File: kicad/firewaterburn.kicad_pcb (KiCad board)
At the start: 2 copper layers, 159.6 x 104.7 mm, 85 parts, among them J1 AudioJack2_SwitchT, J2 AudioJack2_SwitchT, J3 AudioJack2_SwitchT, J4 AudioJack2_SwitchT, J5 AudioJack2_SwitchT, J6 AudioJack2_SwitchT, J7 R61529 LCD, J9 Conn_01x03, P1 USB_C_Plug_USB2.0, Q1 DMN61D9UWQ-13, Q2 DMP31D0U-7, Q3 SS8050-G, Q4 SS8050-G, Q6 DMN2004WK-7, SW1 SW_MEC_5G, SW2 SW_MEC_5G, U1 RT9471GQW, U2 MCP1663T-E/MNY, U3 MCP1603-330I/MC, U4 ESP32-S3-Rx, U5 CP2102N-Axx-xQFN28

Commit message: route complete pcb
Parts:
- removed J9: Conn_01x03, z_connector:Molex_KK-254_AE-6410-03A_1x03_P2.54mm_Vertical
- removed JP2: SolderJumper_3_Open, Jumper:SolderJumper-3_P1.3mm_Open_Pad1.0x1.5mm_NumberLabels
- removed Q6: DMN2004WK-7, Package_TO_SOT_SMD:SOT-323_SC-70
- removed R42, R43: 0R, Resistor_SMD:R_0603_1608Metric
- added J8: R61529 LCD, z_connector:FPC_BOTTOM_20POS_Würth_68712014522, F.Cu at (176.2, 115.0)
- added Q5: DMN2004WK-7, Package_TO_SOT_SMD:SOT-323_SC-70, F.Cu at (103.9, 91.8)
- added R30: 0R, Resistor_SMD:R_0603_1608Metric, F.Cu at (122.7, 130.0)
- added R31: 0R, Resistor_SMD:R_0603_1608Metric, F.Cu at (117.0, 130.0)
- added R32: 10k, Resistor_SMD:R_0603_1608Metric, F.Cu at (163.6, 122.8)
- J3: value AudioJack2_SwitchT -> Conn_01x03; footprint z_connector:MJ-2523 -> z_connector:Molex_KK-254_AE-6410-03A_1x03_P2.54mm_Vertical
- J7: value R61529 LCD -> AudioJack2_SwitchT; footprint z_connector:62684-402100ALF -> z_connector:MJ-2523
- R10, R12: value 3k4 -> 4k42
- R11: value 4k42 -> 3k4
- R13, R17: value 10k -> 3k4
- R18: value 5k23 -> 10k
- R19: value 30k1 -> 0R
- R20: value 2k2 -> 5k23
- R21: value 2k2 -> 30k1
- R22: value 1050k -> 2k2
- R23: value 120k -> 2k2
- R24, R25: value 10k -> 0R
- R26: value 0R -> 1050k
- R27: value 0R -> 120k
- R29, R41: value 0R -> 10k
- R33: value 22k1 -> 0R
- R34: value 47k5 -> 0R
- R35: value 2k -> 22k1
- R36: value 1M -> 47k5
- R37: value 10k -> 2k
- R38: value 3k4 -> 0R
- R40: value 0R -> 1M
- R9: value 4k42 -> 10k
- U1: footprint Package_DFN_QFN:WQFN-24-1EP_4x4mm_P0.5mm_EP2.6x2.6mm_ThermalVias -> z_ic:WQFN-24-1EP_4x4mm_P0.5mm_EP2.6x2.6mm_ThermalVias
- moved R35 92.8 mm to (105.4, 82.8)
- moved R37 88.7 mm to (105.4, 86.0)
- moved C14 88.3 mm to (107.0, 80.2), turned to 90 degrees
- moved R16 87.1 mm to (181.4, 68.3), turned to 90 degrees
- moved D1 86.6 mm to (111.8, 75.0)
- moved R19 85.8 mm to (112.6, 112.2), turned to 90 degrees
- moved R41 85.4 mm to (102.3, 89.2), turned to 180 degrees
- moved R36 84.4 mm to (105.4, 84.4), turned to 180 degrees
- moved U5 83.2 mm to (111.2, 85.9), turned to -90 degrees
- moved C3 80.4 mm to (110.0, 105.5), turned to 90 degrees
- moved P1 80.4 mm to (111.8, 65.2)
- moved C13 80.1 mm to (108.6, 80.2), turned to 90 degrees
- moved R2 76.6 mm to (132.1, 121.2), turned to -90 degrees
- moved C2 75.8 mm to (109.2, 109.8), turned to 180 degrees
- moved R15 74.8 mm to (169.4, 65.2), turned to 90 degrees
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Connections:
- J4 pad T: /OUTPUT/probe5 -> /OUTPUT/probe2
- J5 pad T: /OUTPUT/probe3 -> /OUTPUT/probe5
- J6 pad T: /OUTPUT/probe6 -> /OUTPUT/probe3
- Q2 pad 3: Net-(J9-Pad2) -> Net-(J3-Pad2)
- R10 pad 1: /OUTPUT/probe2 -> +3V3
- R10 pad 2: GND -> /OUTPUT/probe2
- R11 pad 1: +3V3 -> /OUTPUT/probe2
- R11 pad 2: /OUTPUT/probe5 -> GND
- R12 pad 1: /OUTPUT/probe5 -> +3V3
- R12 pad 2: GND -> /OUTPUT/probe5
- R13 pad 1: +3V3 -> /OUTPUT/probe5
- R13 pad 2: /OUTPUT/TACHO -> GND
- R17 pad 1: /mcu_n_tft/CHR_INT -> /OUTPUT/probe6
- R17 pad 2: +3V3 -> GND
- R18 pad 1: Net-(C5-Pad1) -> /mcu_n_tft/CHR_INT
- R18 pad 2: Net-(R18-Pad2) -> +3V3
- R19 pad 1: Net-(R18-Pad2) -> VBUS
- R19 pad 2: GND -> Net-(C1-Pad1)
- R20 pad 1: Net-(D2-Pad1) -> Net-(C5-Pad1)
- R20 pad 2: /power unit/STAT -> Net-(R20-Pad2)
- R21 pad 1: Net-(D3-Pad1) -> Net-(R20-Pad2)
- R21 pad 2: /power unit/~{PG} -> GND
- R22 pad 1: +12V -> Net-(D2-Pad1)
- R22 pad 2: Net-(R22-Pad2) -> /power unit/STAT
- R23 pad 1: Net-(R22-Pad2) -> Net-(D3-Pad1)
- R23 pad 2: GND -> /power unit/~{PG}
- R24 pad 1: Net-(Q3-Pad1) -> VAA
- R24 pad 2: /USB<->UART/DTS -> Net-(C6-Pad1)
- R25 pad 1: Net-(Q4-Pad1) -> VS
- R25 pad 2: /mcu_n_tft/RTS -> Net-(C7-Pad1)
- R26 pad 1: /mcu_n_tft/EN -> +12V
- R26 pad 2: Net-(Q3-Pad3) -> Net-(R26-Pad2)
- R27 pad 1: /mcu_n_tft/BOOT -> Net-(R26-Pad2)
- R27 pad 2: Net-(Q4-Pad3) -> GND
- R28 pad 1: +3V3 -> Net-(Q3-Pad1)
- R28 pad 2: /mcu_n_tft/EN -> /USB<->UART/DTS
- R29 pad 1: Net-(R29-Pad1) -> Net-(Q4-Pad1)
- R29 pad 2: +3V3 -> /mcu_n_tft/RTS
- R33 pad 1: VBUS -> Net-(R33-Pad1)
- R33 pad 2: Net-(R33-Pad2) -> +3V3
- R34 pad 1: Net-(R33-Pad2) -> +3V3
- R34 pad 2: GND -> Net-(J8-Pad1)
- R35 pad 1: +3V3 -> VBUS
- R36 pad 1: GND -> Net-(R35-Pad2)
- R36 pad 2: Net-(Q6-Pad1) -> GND
- R37 pad 1: /USB<->UART/CHREN -> +3V3
- R37 pad 2: VBUS -> Net-(R37-Pad2)
- R38 pad 1: /OUTPUT/probe6 -> +3V3
- R38 pad 2: GND -> Net-(R38-Pad2)
- R39 pad 1: VBUS -> Net-(Q5-Pad1)
- R39 pad 2: Net-(C1-Pad1) -> /USB<->UART/CHREN_
- R40 pad 1: VAA -> GND
- R40 pad 2: Net-(C6-Pad1) -> Net-(Q5-Pad1)
- R41 pad 1: VS -> /USB<->UART/CHREN
- R41 pad 2: Net-(C7-Pad1) -> VBUS
- R9 pad 2: /OUTPUT/probe2 -> /OUTPUT/TACHO
- TH1 pad 1: Net-(R18-Pad2) -> Net-(R20-Pad2)
- U1 pad 11: Net-(R18-Pad2) -> Net-(R20-Pad2)
- U2 pad 1: Net-(R22-Pad2) -> Net-(R26-Pad2)
- U4 pad 12: /OUTPUT/probe5 -> /OUTPUT/probe4
- U4 pad 17: /OUTPUT/probe6 -> /OUTPUT/probe1
- U4 pad 18: /OUTPUT/TACHO -> /OUTPUT/PWM
- U4 pad 19: /OUTPUT/PWM -> /OUTPUT/TACHO
- U4 pad 2: Net-(R29-Pad1) -> Net-(R33-Pad1)
- U4 pad 23: /mcu_n_tft/~{PD} -> /USB<->UART/CHR1
- U4 pad 4: /OUTPUT/probe1 -> /OUTPUT/probe6
- U4 pad 5: /OUTPUT/probe2 -> /OUTPUT/probe3
- U4 pad 6: /OUTPUT/probe3 -> /OUTPUT/probe5
- U4 pad 7: /OUTPUT/probe4 -> /OUTPUT/probe2
- U4 pad 8: /USB<->UART/CHR1 -> /mcu_n_tft/~{PD}
- U5 pad 6: Net-(JP2-Pad2) -> Net-(R38-Pad2)
- U5 pad 8: Net-(R33-Pad2) -> Net-(R35-Pad2)
- U5 pad 9: Net-(R35-Pad2) -> Net-(R37-Pad2)
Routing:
- net GND: track 0.00 -> 527.7 mm, vias 0 -> 40
- net +3V3: track 0.00 -> 245.0 mm, vias 0 -> 17
- net /OUTPUT/probe1: track 0.00 -> 95.1 mm
- net /OUTPUT/probe4: track 0.00 -> 80.7 mm, vias 0 -> 2
- net VBUS: track 0.00 -> 79.0 mm, vias 0 -> 2
- net /mcu_n_tft/RTS: track 0.00 -> 78.1 mm, vias 0 -> 2
- net /OUTPUT/probe2: track 0.00 -> 75.5 mm, vias 0 -> 2
- net /USB<->UART/DTS: track 0.00 -> 72.5 mm, vias 0 -> 2
- net /OUTPUT/probe6: track 0.00 -> 69.0 mm, vias 0 -> 2
- net /OUTPUT/probe5: track 0.00 -> 66.3 mm, vias 0 -> 2
- net VAA: track 0.00 -> 65.7 mm, vias 0 -> 7
- net /OUTPUT/probe3: track 0.00 -> 62.9 mm, vias 0 -> 2
- net /USB<->UART/RXD: track 0.00 -> 59.0 mm
- net /USB<->UART/TXD: track 0.00 -> 58.3 mm
- net /USB<->UART/CHR1: track 0.00 -> 50.5 mm, vias 0 -> 2
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- added copper zone on F.Cu, net +3V3
- added copper zone on B.Cu, net GND
- added copper zone on F.Cu, net GND
- added copper zone on F.Cu, net Net-(C1-Pad1)
- added copper zone on F.Cu, net Net-(C3-Pad1)
- added copper zone on F.Cu, net Net-(C3-Pad2)
- added copper zone on F.Cu, net Net-(C6-Pad1)
- added copper zone on F.Cu, net Net-(C7-Pad1)
- added copper zone on F.Cu, net Net-(D4-Pad2)
- added copper zone on B.Cu, net VAA
- added copper zone on F.Cu, net VAA
- added copper zone on F.Cu, net VS
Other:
- board size 159.6 x 104.7 mm -> 106 x 79.3 mm

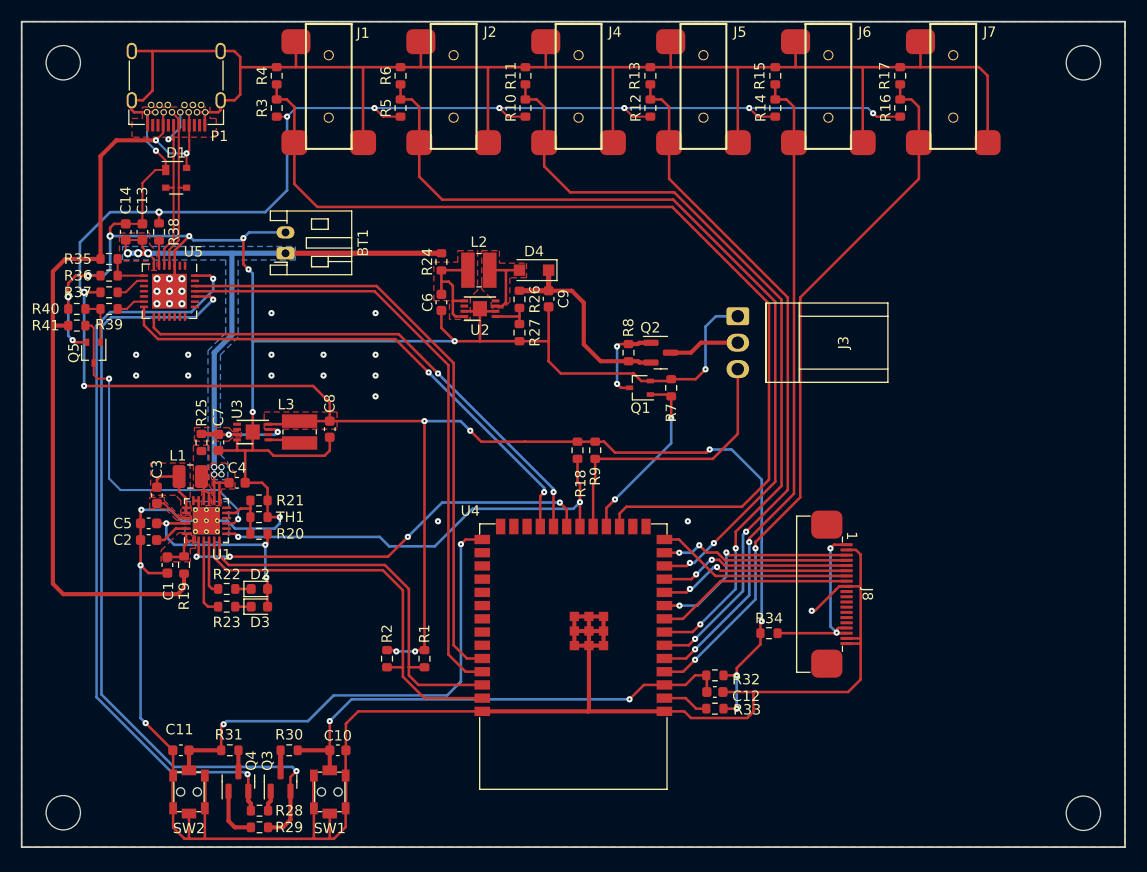
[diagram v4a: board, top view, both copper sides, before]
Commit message: add FreeCAD model for enclosure
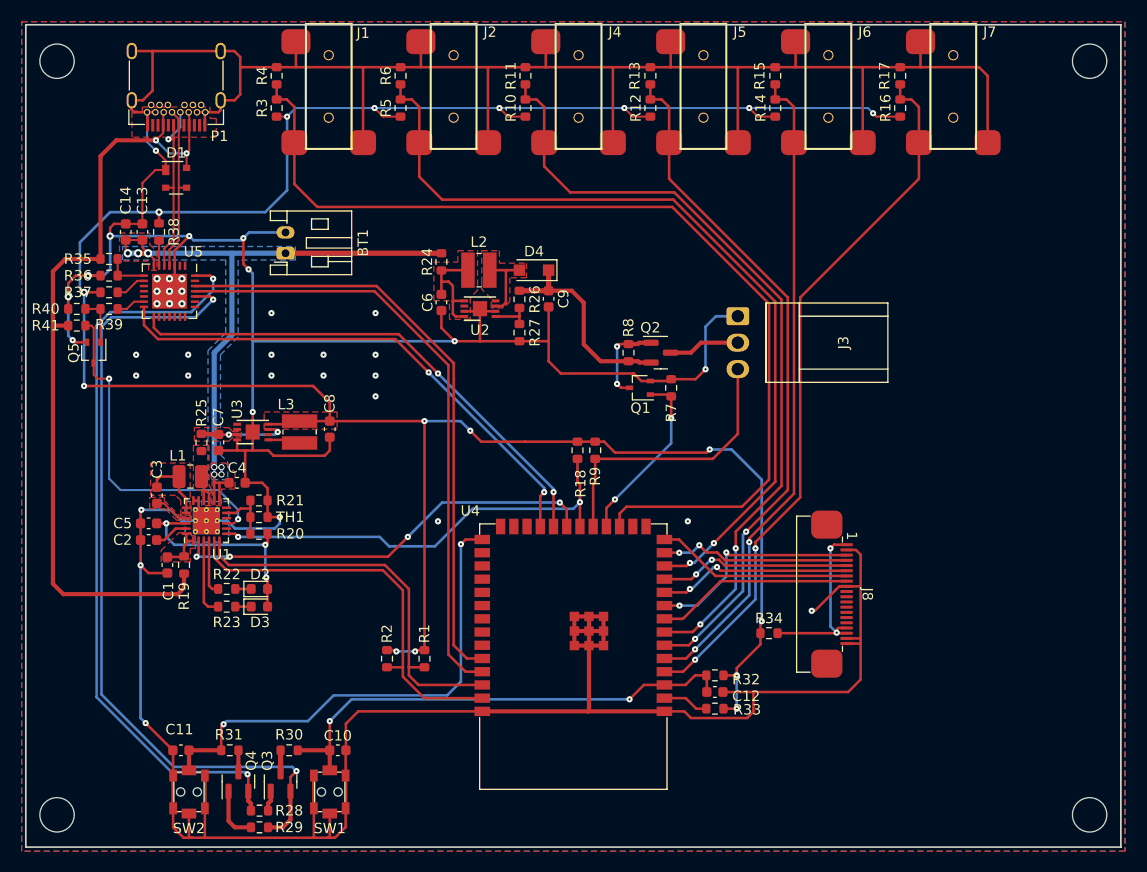
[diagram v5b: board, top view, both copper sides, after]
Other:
- board size 106 x 79.3 mm -> 105.2 x 79 mm

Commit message: rework pcb
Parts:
- removed C10, C11, C12: 100n, Capacitor_SMD:C_0603_1608Metric
- removed Q3, Q4: SS8050-G, Package_TO_SOT_SMD:SOT-23
- removed R28, R29, R32: 10k, Resistor_SMD:R_0603_1608Metric
- removed R30, R31, R33: 0R, Resistor_SMD:R_0603_1608Metric
- removed SW1, SW2: SW_MEC_5G, z_connector:PTS820J25MSMTRLFS
- J1, J2, J4, J5, J6, J7: footprint z_connector:MJ-2523 -> mylib_connector:MJ-2523
- J8: value R61529 LCD -> RVT50HQBNWC00; footprint z_connector:FPC_BOTTOM_20POS_Würth_68712014522 -> mylib_connector:FPC_BOTTOM_20POS_Würth_68712014522
- P1: footprint z_connector:USB_C_Receptacle_Amphenol_12401548E4-2A -> mylib_connector:USB_C_Receptacle_Amphenol_12401548E4-2A
- U1: footprint z_ic:WQFN-24-1EP_4x4mm_P0.5mm_EP2.6x2.6mm_ThermalVias -> mylib_ic:WQFN-24-1EP_4x4mm_P0.5mm_EP2.6x2.6mm_ThermalVias
- U4: value ESP32-S3-Rx -> BL654; footprint z_ic:ESP32-S3-WROOM-1 -> mylib_ic:BL654
- moved U4 38.1 mm to (111.9, 122.9), turned to -90 degrees
- moved J8 9.31 mm to (185.6, 115.2)
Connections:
- J8 pad 11: unconnected-(J8-Pad11) -> /mcu_n_tft/QSPI_IO2
- J8 pad 12: unconnected-(J8-Pad12) -> /mcu_n_tft/QSPI_IO3
- J8 pad 3: /mcu_n_tft/SPICLK -> /mcu_n_tft/QSPI_CLK
- J8 pad 4: /mcu_n_tft/SPIQ -> /mcu_n_tft/QSPI_IO1
- J8 pad 5: /mcu_n_tft/SPID -> /mcu_n_tft/QSPI_IO0
- J8 pad 6: /mcu_n_tft/SPICS0 -> /mcu_n_tft/QSPI_~{CS}
- J8 pad 9: GND -> /tft/GPIO0.0
- R1 pad 2: /mcu_n_tft/SDA -> /power unit/CHARGER_SDA
- R18 pad 1: /mcu_n_tft/CHR_INT -> /power unit/CHARGER_~{INT}
- R2 pad 2: /mcu_n_tft/SCL -> /power unit/CHARGER_SCL
- U1 pad 2: /mcu_n_tft/CHR_PSEL -> /power unit/CHARGER_PSEL
- U1 pad 5: /mcu_n_tft/SCL -> /power unit/CHARGER_SCL
- U1 pad 6: /mcu_n_tft/SDA -> /power unit/CHARGER_SDA
- U1 pad 7: /mcu_n_tft/CHR_INT -> /power unit/CHARGER_~{INT}
- U4 pad 1: GND -> unconnected-(U4-Pad1)
- U4 pad 10: /mcu_n_tft/SPICS0 -> unconnected-(U4-Pad10)
- U4 pad 11: /mcu_n_tft/SPID -> unconnected-(U4-Pad11)
- U4 pad 12: /OUTPUT/probe4 -> unconnected-(U4-Pad12)
- U4 pad 13: /mcu_n_tft/SPIQ -> unconnected-(U4-Pad13)
- U4 pad 14: /mcu_n_tft/~{INT} -> unconnected-(U4-Pad14)
- U4 pad 17: /OUTPUT/probe1 -> unconnected-(U4-Pad17)
- U4 pad 18: /OUTPUT/PWM -> unconnected-(U4-Pad18)
- U4 pad 19: /OUTPUT/TACHO -> unconnected-(U4-Pad19)
- U4 pad 2: Net-(R33-Pad1) -> unconnected-(U4-Pad2)
- U4 pad 20: /mcu_n_tft/CHR_INT -> unconnected-(U4-Pad20)
- U4 pad 21: /mcu_n_tft/CHR_PSEL -> unconnected-(U4-Pad21)
- U4 pad 22: /USB<->UART/CHR0 -> /mcu_n_tft/~{PD}
- U4 pad 23: /USB<->UART/CHR1 -> GND
- U4 pad 26: unconnected-(U4-Pad26) -> GND
- U4 pad 27: /mcu_n_tft/BOOT -> /mcu_n_tft/~{INT}
- U4 pad 28: unconnected-(U4-Pad28) -> /mcu_n_tft/QSPI_CLK
- U4 pad 29: unconnected-(U4-Pad29) -> /mcu_n_tft/QSPI_~{CS}
- U4 pad 3: /mcu_n_tft/EN -> unconnected-(U4-Pad3)
- U4 pad 33: unconnected-(U4-Pad33) -> GND
- U4 pad 35: unconnected-(U4-Pad35) -> /mcu_n_tft/QSPI_IO3
- U4 pad 36: /USB<->UART/TXD -> /mcu_n_tft/QSPI_IO2
- U4 pad 37: /USB<->UART/RXD -> /mcu_n_tft/QSPI_IO1
- U4 pad 38: /mcu_n_tft/SDA -> /mcu_n_tft/QSPI_IO0
- U4 pad 39: /mcu_n_tft/SCL -> unconnected-(U4-Pad39)
- U4 pad 4: /OUTPUT/probe6 -> unconnected-(U4-Pad4)
- U4 pad 41: GND -> unconnected-(U4-Pad41)
- U4 pad 5: /OUTPUT/probe3 -> unconnected-(U4-Pad5)
- U4 pad 6: /OUTPUT/probe5 -> unconnected-(U4-Pad6)
- U4 pad 7: /OUTPUT/probe2 -> unconnected-(U4-Pad7)
- U4 pad 8: /mcu_n_tft/~{PD} -> unconnected-(U4-Pad8)
- U4 pad 9: /mcu_n_tft/SPICLK -> unconnected-(U4-Pad9)
- U5 pad 24: /mcu_n_tft/RTS -> /USB<->UART/RTS
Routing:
- net GND: track 527.7 -> 307.0 mm, vias 40 -> 12
- net /OUTPUT/probe1: track 95.1 -> 6.88 mm
- net /mcu_n_tft/RTS: track 78.1 -> 0.00 mm, vias 2 -> 0
- net /OUTPUT/probe4: track 80.7 -> 6.98 mm, vias 2 -> 0
- net /USB<->UART/DTS: track 72.5 -> 0.00 mm, vias 2 -> 0
- net /OUTPUT/probe2: track 75.5 -> 6.98 mm, vias 2 -> 0
- net /OUTPUT/probe6: track 69.0 -> 6.98 mm, vias 2 -> 0
- net /OUTPUT/probe5: track 66.3 -> 6.98 mm, vias 2 -> 0
- net /USB<->UART/RXD: track 59.0 -> 0.00 mm
- net /USB<->UART/TXD: track 58.3 -> 0.00 mm
- net /OUTPUT/probe3: track 62.9 -> 6.98 mm, vias 2 -> 0
- net /USB<->UART/CHR1: track 50.5 -> 0.00 mm, vias 2 -> 0
- net /USB<->UART/CHR0: track 49.5 -> 0.00 mm, vias 2 -> 0
- net /mcu_n_tft/BOOT: track 47.6 -> 0.00 mm, vias 2 -> 0
- net /mcu_n_tft/EN: track 47.4 -> 0.00 mm, vias 2 -> 0
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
